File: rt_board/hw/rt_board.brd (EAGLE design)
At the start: 100 x 80 mm, 65 parts, among them IC1 MCP170333MB, IC2/L1 TLE4935L, IC3/L1 TLE4935L, IC4/L1 TLE4935L, IC5/L1 TLE4935L, Q1 8MHz, SW1 B3U-1000PM-B, SW2 B3U-1000PM-B, U1 DRV8801PWP, U2 DRV8801PWP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

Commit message: minor fixes suggested by the tool
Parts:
- SV2: value (none) -> SWD
- renumbered SWD to SV2
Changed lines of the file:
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@@
 <element name="L1" library="rcl" package="L2012C" value="10uH" x="21.59" y="38.1"/>
 <element name="C17" library="rcl" package="C1206" value="100nF" x="21.59" y="40.64" rot="R180"/>
-<element name="SWD" library="con-lstb" package="MA06-1" value="" x="39.37" y="53.34">
+<element name="SV2" library="con-lstb" package="MA06-1" value="SWD" x="39.37" y="53.34">
 <attribute name="OC_NEWARK" value="unknown" x="39.37" y="53.34" size="1.778" layer="27" display="off"/>
 <attribute name="MPN" value="" x="39.37" y="53.34" size="1.778" layer="27" display="off"/>
@@
 <contactref element="U6" pad="31"/>
 <contactref element="C17" pad="2"/>
-<contactref element="SWD" pad="3"/>
+<contactref element="SV2" pad="3"/>
 <contactref element="R16" pad="1"/>
 <contactref element="SV1" pad="6"/>
@@
 <contactref element="U6" pad="32"/>
 <contactref element="L1" pad="1"/>
-<contactref element="SWD" pad="1"/>
+<contactref element="SV2" pad="1"/>
 <contactref element="R15" pad="2"/>
 <contactref element="U3" pad="16"/>
@@
 <contactref element="R14" pad="2"/>
 <contactref element="C13" pad="1"/>
-<contactref element="SWD" pad="5"/>
+<contactref element="SV2" pad="5"/>
 <contactref element="SW2" pad="P$2"/>
 <wire x1="20.19" y1="57.15" x2="20.19" y2="55.16" width="0.4064" layer="1"/>
@@
 </signal>
 <signal name="N$4">
-<contactref element="SWD" pad="2"/>
+<contactref element="SV2" pad="2"/>
 <contactref element="U6" pad="49"/>
 <contactref element="R16" pad="2"/>
@@
 <signal name="N$9">
 <contactref element="U6" pad="46"/>
-<contactref element="SWD" pad="4"/>
+<contactref element="SV2" pad="4"/>
 <contactref element="R15" pad="1"/>
 <wire x1="41.06" y1="57.15" x2="41.06" y2="53.76" width="0.4064" layer="1"/>
@@
 </signal>
 </signals>
+<errors>
+</errors>
 </board>
 </drawing>

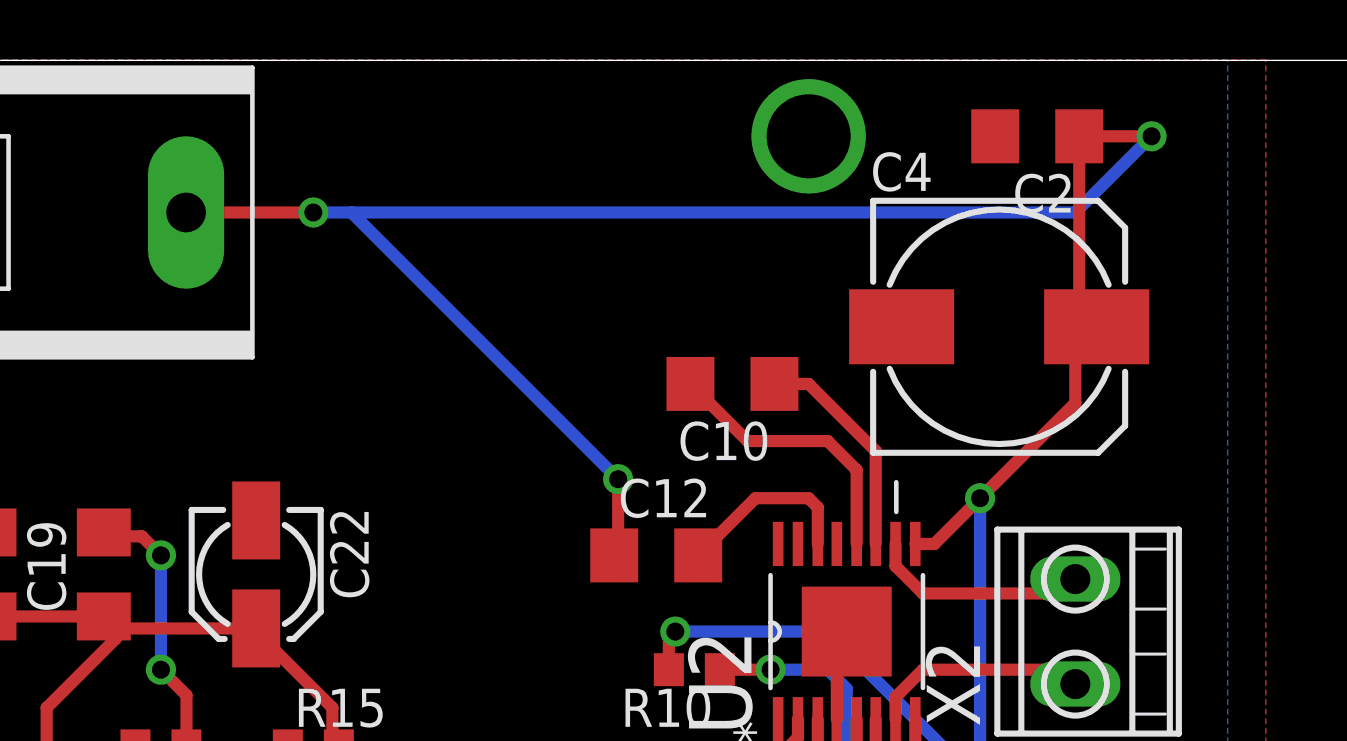
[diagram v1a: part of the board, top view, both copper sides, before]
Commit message: small track optimizations
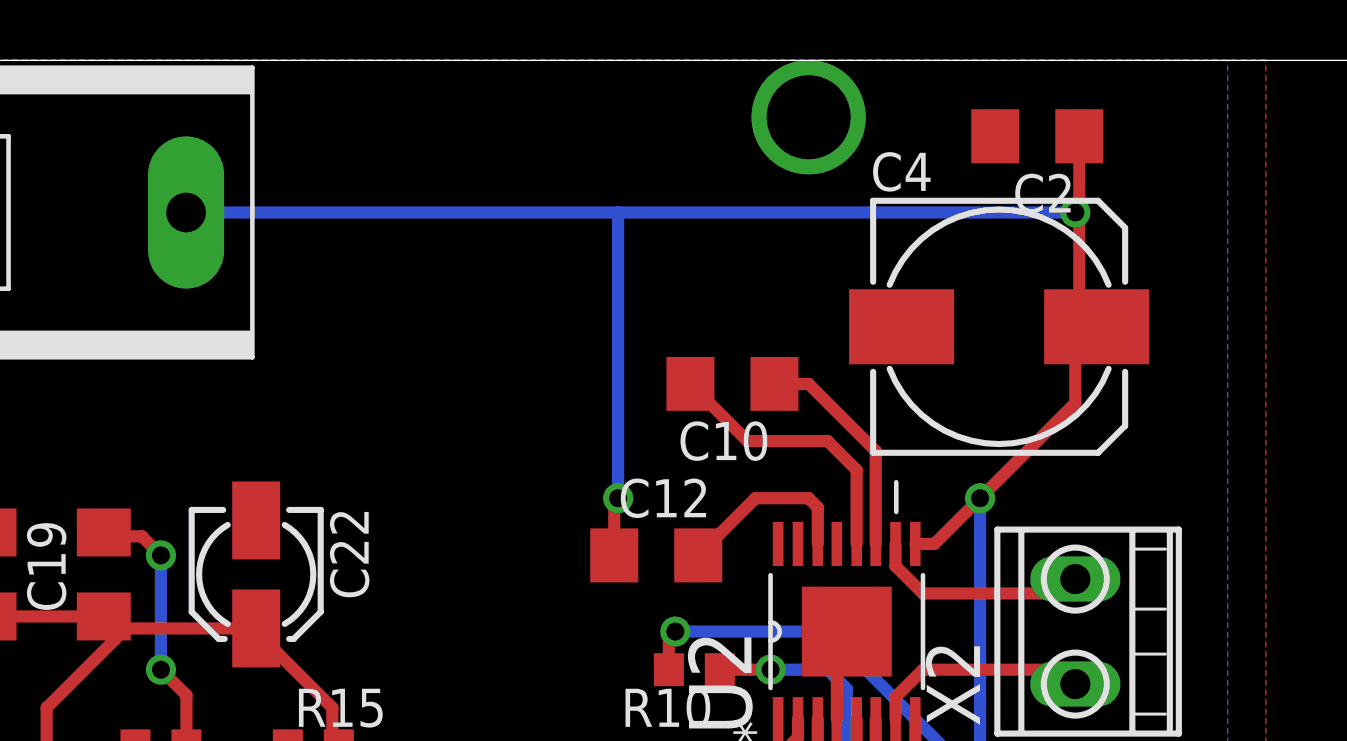
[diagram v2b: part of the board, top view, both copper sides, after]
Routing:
- net +12V: track 133.0 -> 124.0 mm, vias 7 -> 6
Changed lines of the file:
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@@
 <wire x1="67.31" y1="70.41" x2="67.665" y2="70.765" width="0.4064" layer="1"/>
 <wire x1="67.665" y1="70.765" x2="68.02" y2="71.12" width="0.4064" layer="1"/>
-<wire x1="67.44" y1="77.47" x2="67.44" y2="70.99" width="0.4064" layer="1"/>
+<wire x1="67.44" y1="77.47" x2="67.44" y2="74.93" width="0.4064" layer="1"/>
+<wire x1="67.44" y1="74.93" x2="67.44" y2="70.99" width="0.4064" layer="1"/>
 <wire x1="67.44" y1="70.99" x2="67.665" y2="70.765" width="0.4064" layer="1"/>
 <wire x1="67.44" y1="40.64" x2="67.44" y2="43.05" width="0.4064" layer="1"/>
@@
 <wire x1="62.611" y1="63.881" x2="64.135" y2="65.405" width="0.4064" layer="1"/>
 <via x="64.135" y="65.405" extent="1-16" drill="0.6"/>
-<wire x1="69.85" y1="77.47" x2="67.945" y2="77.47" width="0.4064" layer="1"/>
 <wire x1="67.945" y1="77.47" x2="67.31" y2="77.6" width="0.4064" layer="1"/>
 <wire x1="67.31" y1="77.6" x2="67.44" y2="77.47" width="0.4064" layer="1"/>
@@
 <via x="62.865" y="28.575" extent="1-16" drill="0.6"/>
 <wire x1="62.865" y1="28.575" x2="63.5" y2="27.94" width="0.4064" layer="1"/>
-<wire x1="37.6682" y1="74.93" x2="41.91" y2="74.93" width="0.4064" layer="1"/>
-<via x="41.91" y="74.93" extent="1-16" drill="0.6"/>
-<wire x1="41.91" y1="74.93" x2="43.18" y2="74.93" width="0.4064" layer="16"/>
-<wire x1="43.18" y1="74.93" x2="52.07" y2="66.04" width="0.4064" layer="16"/>
-<via x="52.07" y="66.04" extent="1-16" drill="0.6"/>
-<wire x1="52.07" y1="66.04" x2="52.07" y2="63.63" width="0.4064" layer="1"/>
-<wire x1="52.07" y1="63.63" x2="51.94" y2="63.5" width="0.4064" layer="1"/>
-<via x="69.85" y="77.47" extent="1-16" drill="0.6"/>
-<wire x1="69.85" y1="77.47" x2="67.31" y2="74.93" width="0.4064" layer="16"/>
-<wire x1="67.31" y1="74.93" x2="43.18" y2="74.93" width="0.4064" layer="16"/>
+<wire x1="37.6682" y1="74.93" x2="52.07" y2="74.93" width="0.4064" layer="16"/>
+<wire x1="52.07" y1="74.93" x2="67.31" y2="74.93" width="0.4064" layer="16"/>
+<wire x1="67.44" y1="74.93" x2="67.31" y2="74.93" width="0.4064" layer="1"/>
+<via x="67.31" y="74.93" extent="1-16" drill="0.6"/>
+<wire x1="51.94" y1="63.5" x2="51.94" y2="65.275" width="0.4064" layer="1"/>
+<wire x1="51.94" y1="65.275" x2="52.07" y2="65.405" width="0.4064" layer="1"/>
+<via x="52.07" y="65.405" extent="1-16" drill="0.6"/>
+<wire x1="52.07" y1="65.405" x2="52.07" y2="74.93" width="0.4064" layer="16"/>
 </signal>
 <signal name="N$2">
@@
 </signal>
 <signal name="N$52">
-<via x="58.42" y="77.47" extent="1-16" drill="2.8"/>
+<via x="58.42" y="78.105" extent="1-16" drill="2.8"/>
 </signal>
 <signal name="N$53">
@@
 </signal>
 </signals>
-<errors>
-</errors>
 </board>
 </drawing>

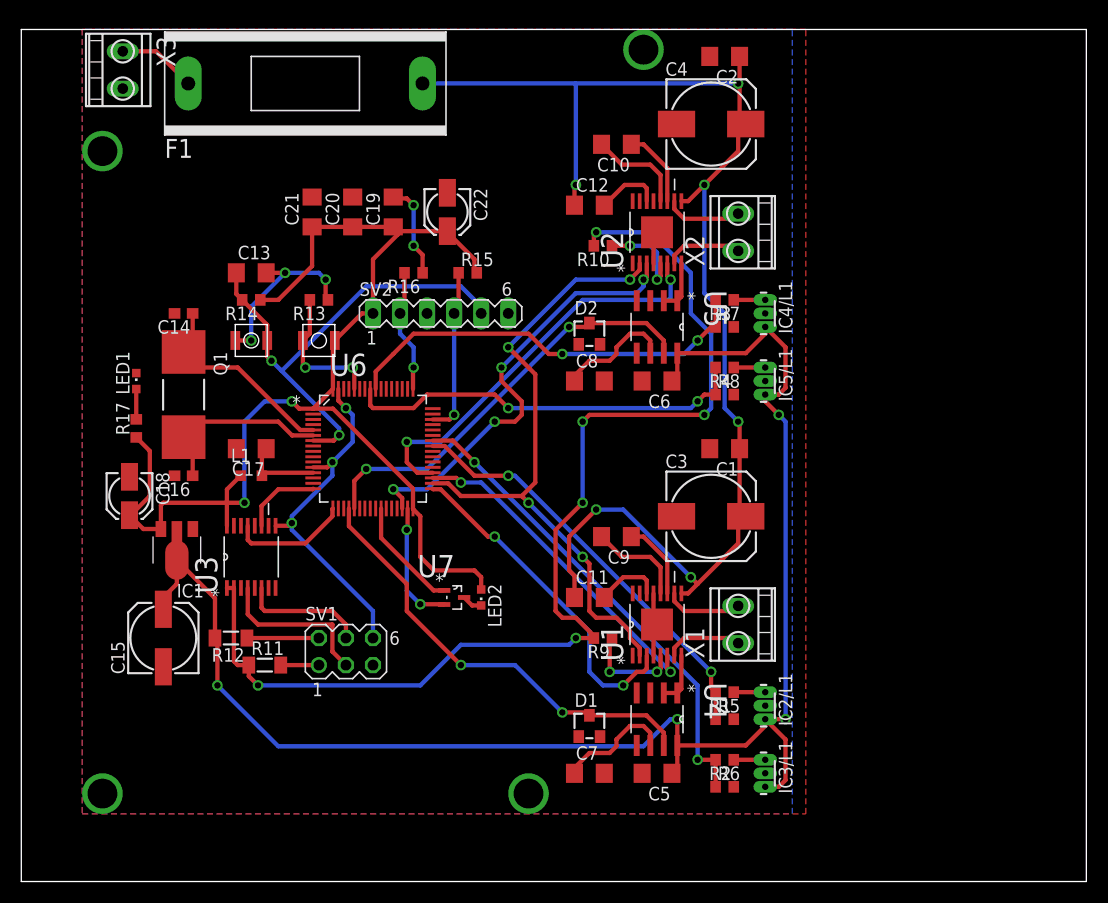
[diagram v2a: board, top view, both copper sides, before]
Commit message: main power routes thickened; montage drills are now connected to GND
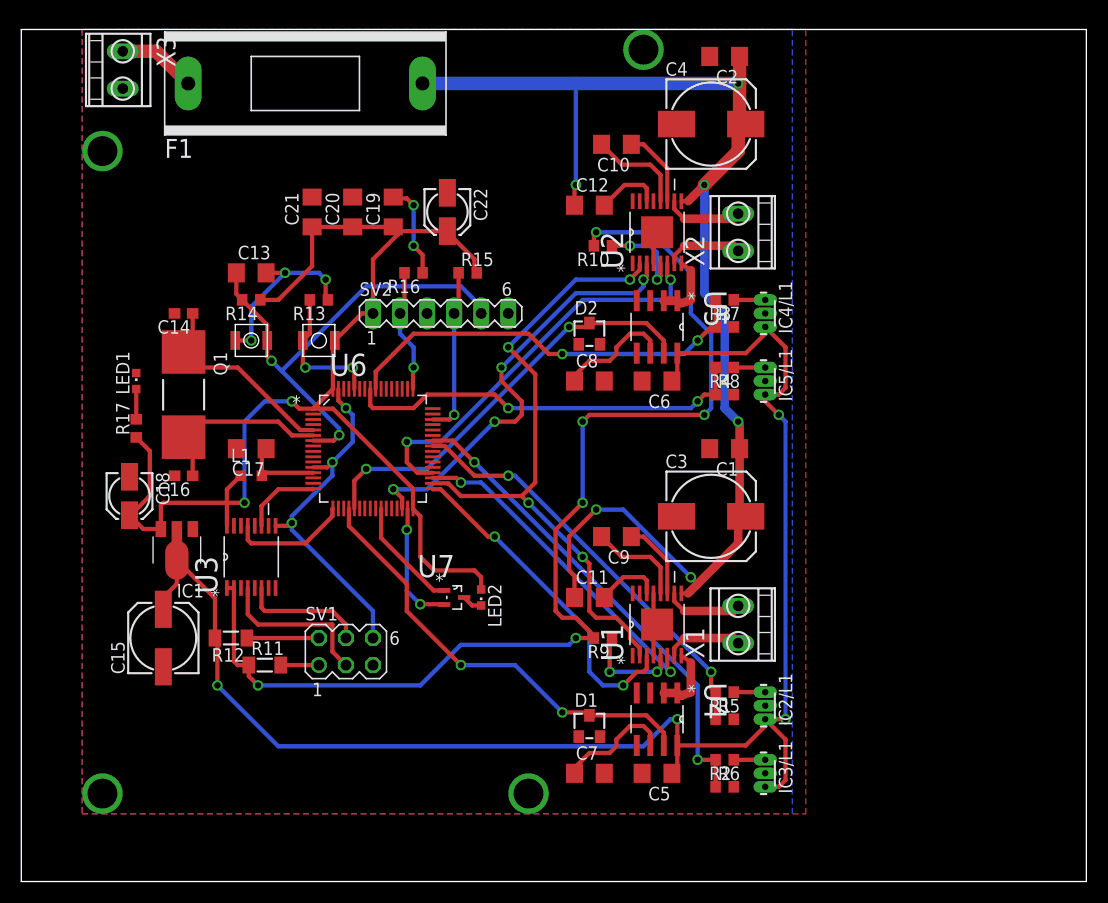
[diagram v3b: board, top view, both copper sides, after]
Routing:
- net N$22: track 4.93 -> 6.56 mm
- net N$36: track 4.93 -> 6.56 mm
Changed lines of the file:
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@@
 <contactref element="C12" pad="1"/>
 <wire x1="61.976" y1="27.051" x2="62.611" y2="27.051" width="0.4064" layer="1"/>
-<wire x1="62.611" y1="27.051" x2="63.5" y2="27.94" width="0.4064" layer="1"/>
-<wire x1="63.5" y1="27.94" x2="67.31" y2="31.75" width="0.4064" layer="1"/>
-<wire x1="67.31" y1="31.75" x2="67.31" y2="33.58" width="0.4064" layer="1"/>
+<wire x1="62.611" y1="27.051" x2="63.5" y2="27.94" width="0.8128" layer="1"/>
+<wire x1="63.5" y1="27.94" x2="67.31" y2="31.75" width="0.8128" layer="1"/>
+<wire x1="67.31" y1="31.75" x2="67.31" y2="33.58" width="0.8128" layer="1"/>
 <wire x1="67.31" y1="33.58" x2="67.665" y2="33.935" width="0.4064" layer="1"/>
 <wire x1="67.665" y1="33.935" x2="68.02" y2="34.29" width="0.4064" layer="1"/>
-<wire x1="67.44" y1="40.64" x2="67.44" y2="34.16" width="0.4064" layer="1"/>
+<wire x1="67.44" y1="40.64" x2="67.44" y2="34.16" width="0.8128" layer="1"/>
 <wire x1="67.44" y1="34.16" x2="67.665" y2="33.935" width="0.4064" layer="1"/>
 <wire x1="61.976" y1="63.881" x2="62.611" y2="63.881" width="0.4064" layer="1"/>
-<wire x1="64.135" y1="65.405" x2="67.31" y2="68.58" width="0.4064" layer="1"/>
-<wire x1="67.31" y1="68.58" x2="67.31" y2="70.41" width="0.4064" layer="1"/>
+<wire x1="64.135" y1="65.405" x2="67.31" y2="68.58" width="1.27" layer="1"/>
+<wire x1="67.31" y1="68.58" x2="67.31" y2="70.41" width="1.27" layer="1"/>
 <wire x1="67.31" y1="70.41" x2="67.665" y2="70.765" width="0.4064" layer="1"/>
 <wire x1="67.665" y1="70.765" x2="68.02" y2="71.12" width="0.4064" layer="1"/>
-<wire x1="67.44" y1="77.47" x2="67.44" y2="74.93" width="0.4064" layer="1"/>
-<wire x1="67.44" y1="74.93" x2="67.44" y2="70.99" width="0.4064" layer="1"/>
+<wire x1="67.44" y1="77.47" x2="67.44" y2="74.93" width="1.27" layer="1"/>
+<wire x1="67.44" y1="74.93" x2="67.44" y2="70.99" width="1.27" layer="1"/>
 <wire x1="67.44" y1="70.99" x2="67.665" y2="70.765" width="0.4064" layer="1"/>
-<wire x1="67.44" y1="40.64" x2="67.44" y2="43.05" width="0.4064" layer="1"/>
+<wire x1="67.44" y1="40.64" x2="67.44" y2="43.05" width="0.8128" layer="1"/>
 <wire x1="67.44" y1="43.05" x2="67.31" y2="43.18" width="0.4064" layer="1"/>
 <via x="67.31" y="43.18" extent="1-16" drill="0.6"/>
-<wire x1="67.31" y1="43.18" x2="66.04" y2="44.45" width="0.4064" layer="16"/>
-<wire x1="66.04" y1="44.45" x2="66.04" y2="53.34" width="0.4064" layer="16"/>
-<wire x1="66.04" y1="53.34" x2="64.135" y2="55.245" width="0.4064" layer="16"/>
-<wire x1="64.135" y1="55.245" x2="64.135" y2="65.405" width="0.4064" layer="16"/>
-<wire x1="62.611" y1="63.881" x2="64.135" y2="65.405" width="0.4064" layer="1"/>
+<wire x1="67.31" y1="43.18" x2="66.04" y2="44.45" width="0.8128" layer="16"/>
+<wire x1="66.04" y1="44.45" x2="66.04" y2="53.34" width="0.8128" layer="16"/>
+<wire x1="66.04" y1="53.34" x2="64.135" y2="55.245" width="0.8128" layer="16"/>
+<wire x1="64.135" y1="55.245" x2="64.135" y2="65.405" width="0.8128" layer="16"/>
+<wire x1="62.611" y1="63.881" x2="64.135" y2="65.405" width="0.8128" layer="1"/>
 <via x="64.135" y="65.405" extent="1-16" drill="0.6"/>
 <wire x1="67.945" y1="77.47" x2="67.31" y2="77.6" width="0.4064" layer="1"/>
@@
 <via x="62.865" y="28.575" extent="1-16" drill="0.6"/>
 <wire x1="62.865" y1="28.575" x2="63.5" y2="27.94" width="0.4064" layer="1"/>
-<wire x1="37.6682" y1="74.93" x2="52.07" y2="74.93" width="0.4064" layer="16"/>
-<wire x1="52.07" y1="74.93" x2="67.31" y2="74.93" width="0.4064" layer="16"/>
+<wire x1="37.6682" y1="74.93" x2="52.07" y2="74.93" width="1.27" layer="16"/>
+<wire x1="52.07" y1="74.93" x2="67.31" y2="74.93" width="1.27" layer="16"/>
 <wire x1="67.44" y1="74.93" x2="67.31" y2="74.93" width="0.4064" layer="1"/>
 <via x="67.31" y="74.93" extent="1-16" drill="0.6"/>
@@
 <contactref element="X3" pad="1"/>
 <contactref element="F1" pad="1"/>
-<wire x1="9.525" y1="77.95" x2="12.6518" y2="77.95" width="0.4064" layer="1"/>
-<wire x1="12.6518" y1="77.95" x2="15.6718" y2="74.93" width="0.4064" layer="1"/>
+<wire x1="9.525" y1="77.95" x2="12.6518" y2="77.95" width="1.27" layer="1"/>
+<wire x1="12.6518" y1="77.95" x2="15.6718" y2="74.93" width="1.27" layer="1"/>
 </signal>
 <signal name="N$5">
@@
 <wire x1="61.3156" y1="21.209" x2="61.3156" y2="21.9456" width="0.4064" layer="1"/>
 <wire x1="61.3156" y1="21.9456" x2="62.23" y2="22.86" width="0.4064" layer="1"/>
-<wire x1="62.23" y1="22.86" x2="66.83" y2="22.86" width="0.4064" layer="1"/>
-<wire x1="66.83" y1="22.86" x2="67.31" y2="22.38" width="0.4064" layer="1"/>
+<wire x1="62.23" y1="22.86" x2="66.83" y2="22.86" width="0.8128" layer="1"/>
+<wire x1="66.83" y1="22.86" x2="67.31" y2="22.38" width="0.8128" layer="1"/>
 </signal>
 <signal name="N$21">
@@
 <wire x1="61.3156" y1="27.051" x2="61.3156" y2="26.3144" width="0.4064" layer="1"/>
 <wire x1="61.3156" y1="26.3144" x2="62.23" y2="25.4" width="0.4064" layer="1"/>
-<wire x1="62.23" y1="25.4" x2="66.83" y2="25.4" width="0.4064" layer="1"/>
-<wire x1="66.83" y1="25.4" x2="67.31" y2="25.88" width="0.4064" layer="1"/>
+<wire x1="62.23" y1="25.4" x2="66.83" y2="25.4" width="0.8128" layer="1"/>
+<wire x1="66.83" y1="25.4" x2="67.31" y2="25.88" width="0.8128" layer="1"/>
 </signal>
 <signal name="N$24">
@@
 <contactref element="U4" pad="2"/>
 <contactref element="U1" pad="8"/>
-<wire x1="61.976" y1="21.209" x2="61.976" y2="18.0848" width="0.4064" layer="1"/>
-<wire x1="61.976" y1="18.0848" x2="61.595" y2="17.7038" width="0.4064" layer="1"/>
-<wire x1="61.595" y1="17.7038" x2="60.325" y2="17.7038" width="0.4064" layer="1"/>
+<wire x1="61.976" y1="21.209" x2="62.865" y2="20.574" width="0.4064" layer="1"/>
+<wire x1="62.865" y1="20.574" x2="62.865" y2="17.78" width="0.8128" layer="1"/>
+<wire x1="62.865" y1="17.78" x2="61.976" y2="17.4498" width="0.8128" layer="1"/>
+<wire x1="61.976" y1="17.4498" x2="61.595" y2="17.7038" width="0.8128" layer="1"/>
+<wire x1="61.595" y1="17.7038" x2="60.325" y2="17.7038" width="0.8128" layer="1"/>
 </signal>
 <signal name="N$23">
@@
 <wire x1="61.3156" y1="58.039" x2="61.3156" y2="58.7756" width="0.4064" layer="1"/>
 <wire x1="61.3156" y1="58.7756" x2="62.23" y2="59.69" width="0.4064" layer="1"/>
-<wire x1="62.23" y1="59.69" x2="66.83" y2="59.69" width="0.4064" layer="1"/>
-<wire x1="66.83" y1="59.69" x2="67.31" y2="59.21" width="0.4064" layer="1"/>
+<wire x1="62.23" y1="59.69" x2="66.83" y2="59.69" width="0.8128" layer="1"/>
+<wire x1="66.83" y1="59.69" x2="67.31" y2="59.21" width="0.8128" layer="1"/>
 </signal>
 <signal name="N$34">
@@
 <wire x1="61.3156" y1="63.881" x2="61.3156" y2="63.1444" width="0.4064" layer="1"/>
 <wire x1="61.3156" y1="63.1444" x2="62.23" y2="62.23" width="0.4064" layer="1"/>
-<wire x1="62.23" y1="62.23" x2="66.83" y2="62.23" width="0.4064" layer="1"/>
-<wire x1="66.83" y1="62.23" x2="67.31" y2="62.71" width="0.4064" layer="1"/>
+<wire x1="62.23" y1="62.23" x2="66.83" y2="62.23" width="0.8128" layer="1"/>
+<wire x1="66.83" y1="62.23" x2="67.31" y2="62.71" width="0.8128" layer="1"/>
 </signal>
 <signal name="N$35">
@@
 <contactref element="U5" pad="2"/>
 <contactref element="U2" pad="8"/>
-<wire x1="61.976" y1="58.039" x2="61.976" y2="54.9148" width="0.4064" layer="1"/>
-<wire x1="61.976" y1="54.9148" x2="61.595" y2="54.5338" width="0.4064" layer="1"/>
-<wire x1="61.595" y1="54.5338" x2="60.325" y2="54.5338" width="0.4064" layer="1"/>
+<wire x1="61.976" y1="58.039" x2="62.865" y2="57.404" width="0.4064" layer="1"/>
+<wire x1="62.865" y1="57.404" x2="62.865" y2="54.61" width="0.8128" layer="1"/>
+<wire x1="62.865" y1="54.61" x2="61.976" y2="54.2798" width="0.8128" layer="1"/>
+<wire x1="61.976" y1="54.2798" x2="61.595" y2="54.5338" width="0.4064" layer="1"/>
+<wire x1="61.595" y1="54.5338" x2="60.325" y2="54.5338" width="0.8128" layer="1"/>
 </signal>
 <signal name="N$37">
